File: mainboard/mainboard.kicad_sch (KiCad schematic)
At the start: 93 parts, among them J1 Eurorack_Power, J2 Inv1, J3 Inv2, J4 Ver2, J5 Ver1, J6 Conn_02x04_Counter_Clockwise, J7 Conn_02x03_Counter_Clockwise, J8 Out2, J9 Out1, Q1 BC557, Q10 BC557, Q11 BC557, Q12 BC557, Q13 BC547, Q14 BC547, Q15 BC557, Q16 BC557, Q17 BC547, Q18 BC547, Q19 BC557, Q2 BC557, Q20 BC557, Q21 BC547, Q22 BC547, Q23 BC557, Q24 BC547, Q25 BC547, Q3 BC547, Q4 BC547, Q5 BC547, Q6 BC547, Q7 BC547, Q8 BC547, Q9 BC557, U1 L78L09_TO92, U2 TL074

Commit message: Routing
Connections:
- net MIDO1: now also U2.6 (-), U2.7; no longer U2.1, U2.2 (-)
- net MIDO2: now also U2.8, U2.9 (-); no longer U2.13 (-), U2.14
- net Out1: now also U2.3 (+); no longer U2.5 (+)
- net at R13.2, R14.1: now also U2.5 (+); no longer U2.3 (+)
- net at C4.1, Q14.1 (C), R30.1: now also U2.12 (+); no longer U2.10 (+)
- net at R15.2, R16.1: now also U2.10 (+); no longer U2.12 (+)
- new net: R34.2, U2.1, U2.2 (-)
- new net: R33.2, U2.13 (-), U2.14
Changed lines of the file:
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@@
     (pin "1")
   )
-  (symbol (lib_id "Amplifier_Operational:TL074") (at 163.83 81.28 0) (unit 2)
+  (symbol (lib_id "Amplifier_Operational:TL074") (at 163.83 81.28 0) (unit 1)
     (in_bom yes) (on_board yes) (fields_autoplaced)
     (property "Reference" "U2" (id 0) (at 163.83 71.12 0))
@@
     (pin "3")
   )
-  (symbol (lib_id "Amplifier_Operational:TL074") (at 105.41 30.48 0) (unit 1)
+  (symbol (lib_id "Amplifier_Operational:TL074") (at 105.41 30.48 0) (unit 2)
     (in_bom yes) (on_board yes) (fields_autoplaced)
     (property "Reference" "U2" (id 0) (at 105.41 20.32 0))
@@
     (pin "6")
   )
-  (symbol (lib_id "Amplifier_Operational:TL074") (at 162.56 163.83 0) (unit 3)
+  (symbol (lib_id "Amplifier_Operational:TL074") (at 162.56 163.83 0) (unit 4)
     (in_bom yes) (on_board yes) (fields_autoplaced)
     (property "Reference" "U2" (id 0) (at 162.56 153.67 0))
@@
     (pin "3")
   )
-  (symbol (lib_id "Amplifier_Operational:TL074") (at 105.41 64.77 0) (unit 4)
+  (symbol (lib_id "Amplifier_Operational:TL074") (at 105.41 64.77 0) (unit 3)
     (in_bom yes) (on_board yes) (fields_autoplaced)
     (property "Reference" "U2" (id 0) (at 105.41 54.61 0))
@@
       (reference "U1") (unit 1) (value "L78L09_TO92") (footprint "Package_TO_SOT_THT:TO-92_Inline")
     )
+    (path "/0ebda1a3-7afe-4b2c-9147-5e2f0fea4082"
+      (reference "U2") (unit 1) (value "TL074") (footprint "Package_DIP:DIP-14_W7.62mm_Socket")
+    )
     (path "/211453b7-cfa5-409e-b9f2-b42bf15d1016"
-      (reference "U2") (unit 1) (value "TL074") (footprint "Package_DIP:DIP-14_W7.62mm_Socket")
-    )
-    (path "/0ebda1a3-7afe-4b2c-9147-5e2f0fea4082"
       (reference "U2") (unit 2) (value "TL074") (footprint "Package_DIP:DIP-14_W7.62mm_Socket")
     )
+    (path "/8cecb3d6-9653-4f3c-a3b3-a8676a225b3c"
+      (reference "U2") (unit 3) (value "TL074") (footprint "Package_DIP:DIP-14_W7.62mm_Socket")
+    )
     (path "/29c5794b-5b31-4263-a1f4-eb1defc43e42"
-      (reference "U2") (unit 3) (value "TL074") (footprint "Package_DIP:DIP-14_W7.62mm_Socket")
-    )
-    (path "/8cecb3d6-9653-4f3c-a3b3-a8676a225b3c"
       (reference "U2") (unit 4) (value "TL074") (footprint "Package_DIP:DIP-14_W7.62mm_Socket")
     )

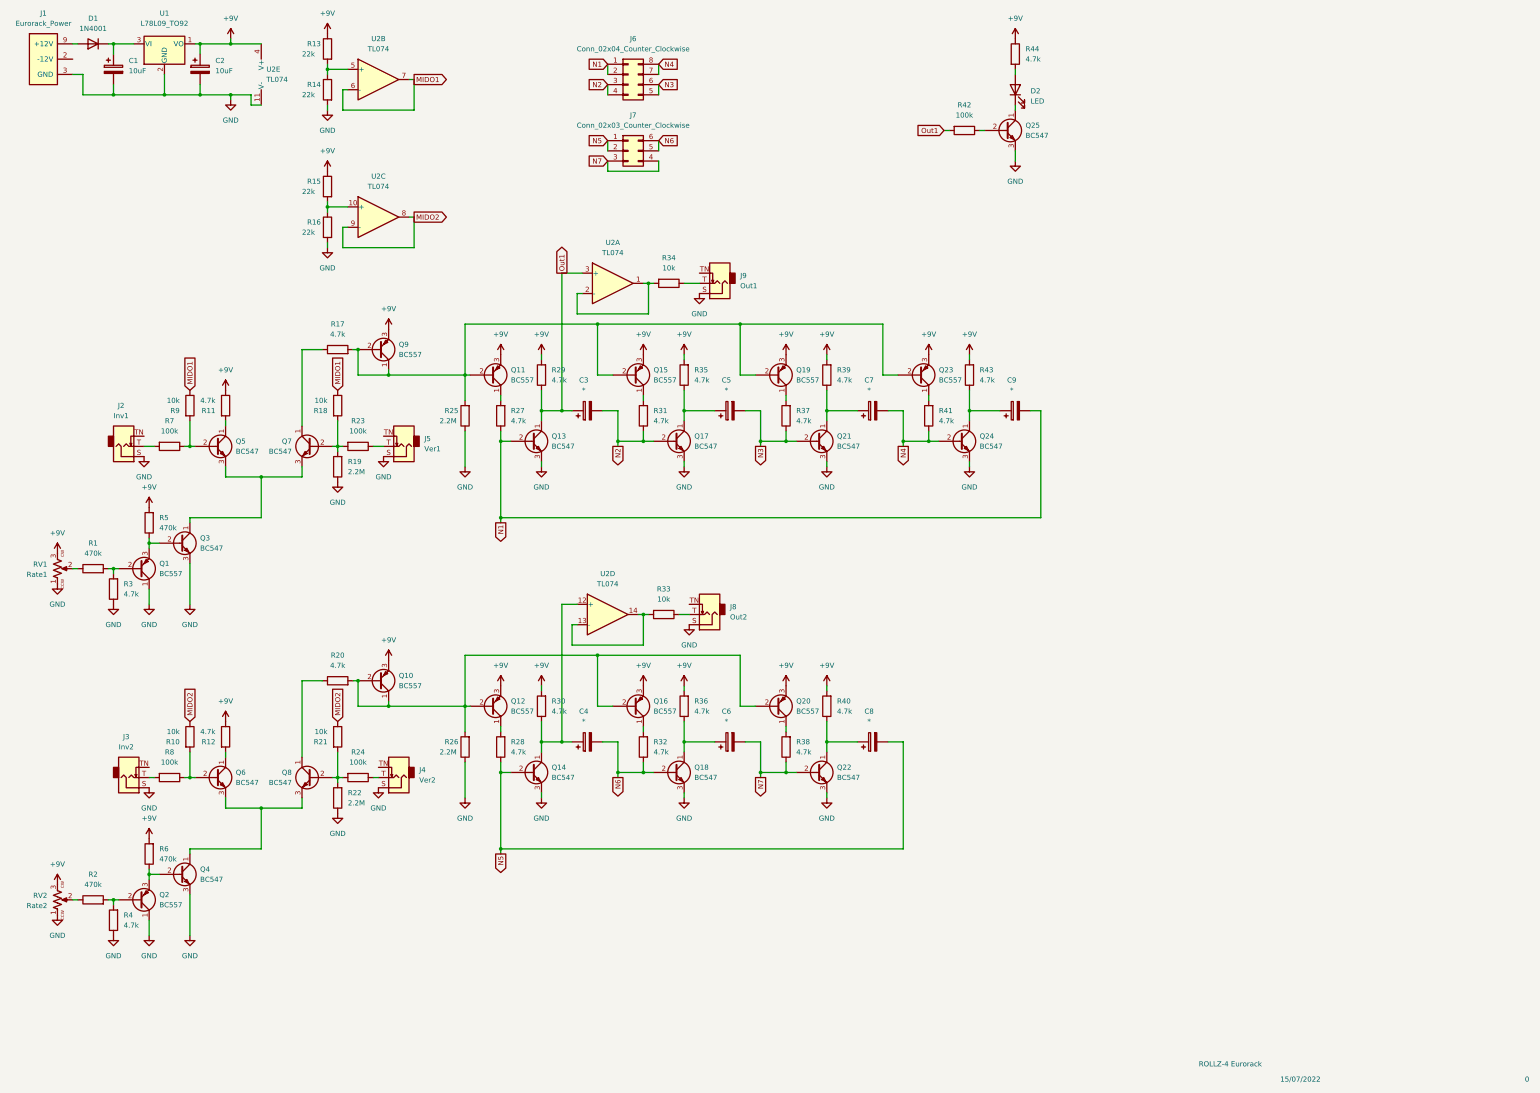
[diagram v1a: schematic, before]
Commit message: Attenuator version
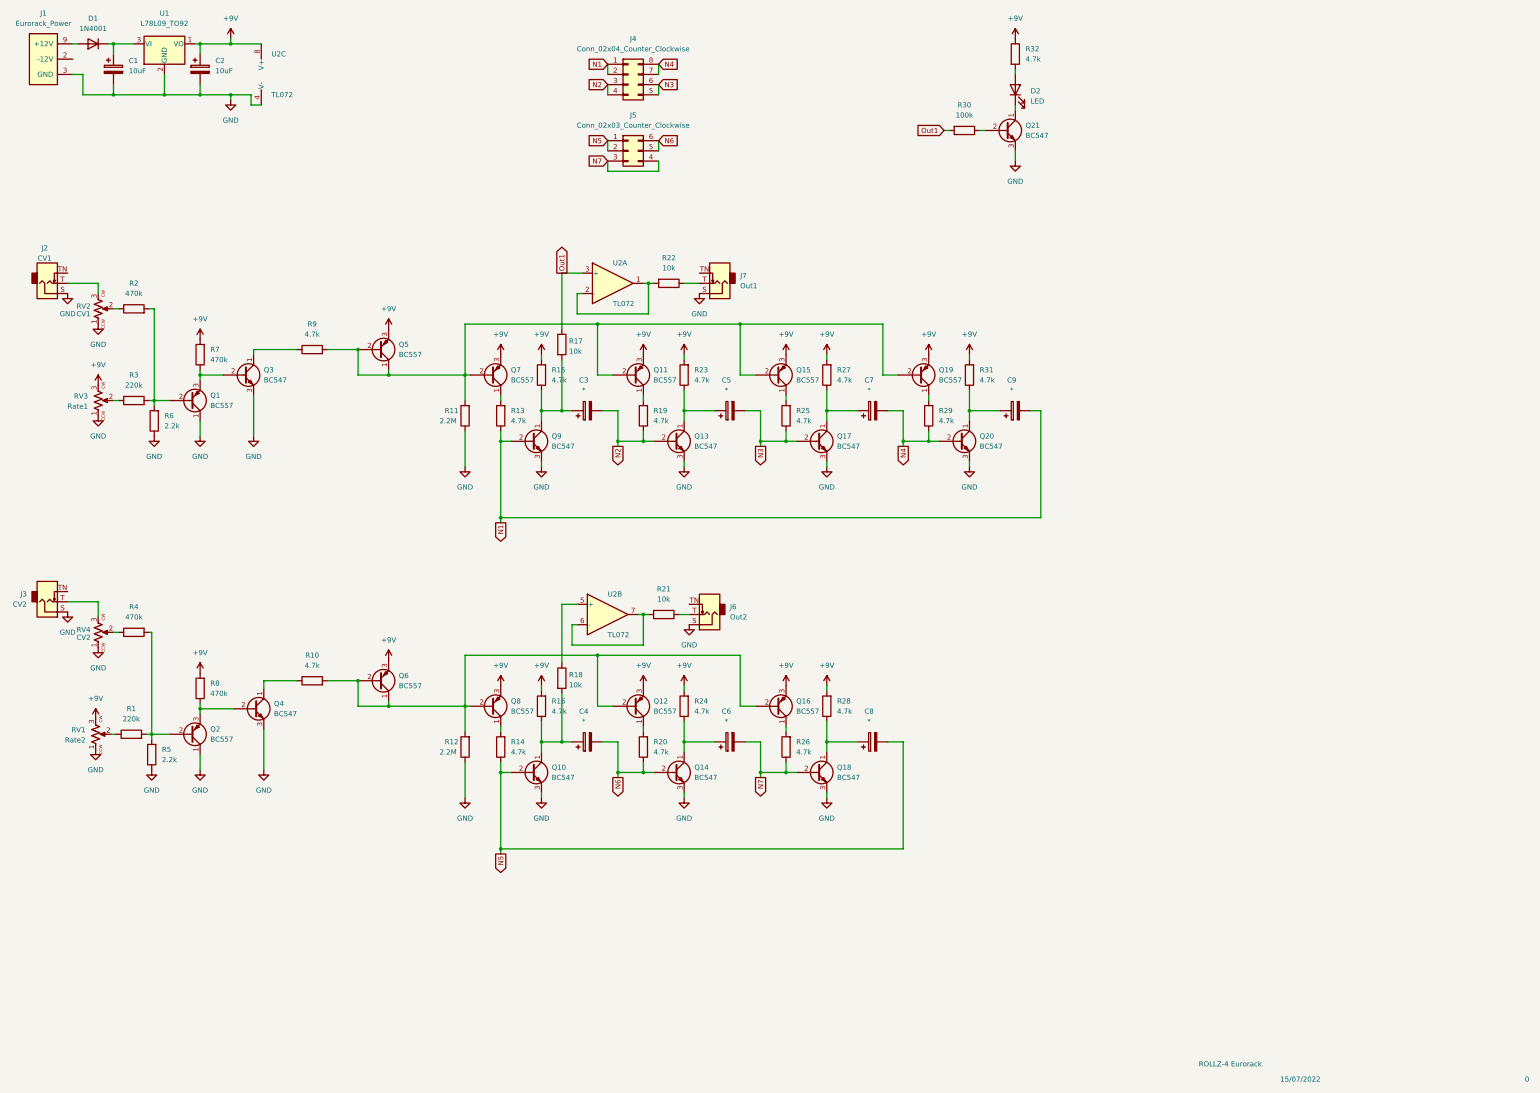
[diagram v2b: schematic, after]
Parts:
- removed J2: Inv1, winterbloom:AudioJack_WQP518MA, symbol winterbloom:Eurorack_Mono_Jack
- removed J3: Inv2, winterbloom:AudioJack_WQP518MA, symbol winterbloom:Eurorack_Mono_Jack
- removed Q5, Q6, Q7, Q8: BC547, Package_TO_SOT_THT:TO-92_Inline, symbol Transistor_BJT:BC547
- removed R10, R21, R9: 10k, Resistor_THT:R_Axial_DIN0204_L3.6mm_D1.6mm_P7.62mm_Horizontal, symbol Device:R
- removed R11, R12: 4.7k, Resistor_THT:R_Axial_DIN0204_L3.6mm_D1.6mm_P7.62mm_Horizontal, symbol Device:R
- removed R13, R14, R15, R16: 22k, Resistor_THT:R_Axial_DIN0204_L3.6mm_D1.6mm_P7.62mm_Horizontal, symbol Device:R
- removed R19, R22: 2.2M, Resistor_THT:R_Axial_DIN0204_L3.6mm_D1.6mm_P7.62mm_Horizontal, symbol Device:R
- removed R23, R7, R8: 100k, Resistor_THT:R_Axial_DIN0204_L3.6mm_D1.6mm_P7.62mm_Horizontal, symbol Device:R
- removed unit 2 of U2
- removed unit 3 of U2
- added R17: 10k, Resistor_THT:R_Axial_DIN0204_L3.6mm_D1.6mm_P7.62mm_Horizontal, symbol Device:R
- added R2: 470k, Resistor_THT:R_Axial_DIN0204_L3.6mm_D1.6mm_P7.62mm_Horizontal, symbol Device:R
- added RV2: CV1, winterbloom:Potentiometer_Alpha_R0904N, symbol winterbloom:Eurorack_Pot
- added RV4: CV2, winterbloom:Potentiometer_Alpha_R0904N, symbol winterbloom:Eurorack_Pot
- J2: renamed from J5; value Ver1 -> CV1
- J3: renamed from J4; value Ver2 -> CV2
- R1: renamed from R2; value 470k -> 220k
- R3: renamed from R1; value 470k -> 220k
- R4: renamed from R24; value 100k -> 470k
- R5: renamed from R4; value 4.7k -> 2.2k
- R6: renamed from R3; value 4.7k -> 2.2k
- U2: value TL074 -> TL072; footprint Package_DIP:DIP-14_W7.62mm_Socket -> Package_DIP:DIP-8_W7.62mm_Socket; symbol Amplifier_Operational:TL074 -> Amplifier_Operational:TL072
- renumbered J6 to J4, J7 to J5, J8 to J6, J9 to J7, Q14 to Q10, Q15 to Q11, Q16 to Q12, Q17 to Q13, Q18 to Q14, Q19 to Q15, Q20 to Q16, Q21 to Q17, Q22 to Q18, Q23 to Q19, Q24 to Q20, Q25 to Q21, Q9 to Q5, Q10 to Q6, Q11 to Q7, Q12 to Q8, Q13 to Q9, R20 to R10, R25 to R11, R26 to R12, R27 to R13, R28 to R14, R29 to R15, R30 to R16, R31 to R19, R32 to R20, R33 to R21, R34 to R22, R35 to R23, R36 to R24, R37 to R25, R38 to R26, R39 to R27, R40 to R28, R41 to R29, R42 to R30, R43 to R31, R44 to R32, R5 to R7, R6 to R8, R17 to R9, RV2 to RV1, RV1 to RV3
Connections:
- net +9V: now also U2.8 (V+); no longer U2.4 (V+)
- net GND: now also U2.4 (V-), RV2.1, RV4.1; no longer U2.11 (V-)
- net Out1: now also R17.1; no longer C3.1, Q9.1 (C), R15.1
- net at Q1.2 (B), R3.2, R6.2: now also R2.2
- net at R4.1: now also RV4.2; no longer J3.T (Tip)
- net at R4.2: now also Q2.2 (B), R1.2, R5.2
- net at R10.1: now also Q4.1 (C)
- net at C4.1, Q10.1 (C), R16.1: now also R18.2; no longer U2.12 (+)
- net at Q3.1 (C): now also R9.1
- net at J2.T (Tip): now also RV2.3
- net MIDO1: no longer names the net of R18.1
- net MIDO1: now also U2.5 (+)
- new net: R2.1, RV2.2
- new net: C3.1, Q9.1 (C), R15.1, R17.2
- new net: R21.2, U2.6 (-), U2.7
- new net: J3.T (Tip), RV4.3
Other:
- moved on the sheet: J2, J3, Q1, Q2, Q3, Q4, R1, R10, R3, R4, R5, R6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

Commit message: Front panel
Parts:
- added D3, D4: BAT85, Diode_THT:D_DO-35_SOD27_P7.62mm_Horizontal, symbol Diode:BAT85
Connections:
- net GND: now also D3.2 (A), D4.2 (A)
- net at J2.T (Tip), RV2.3: now also D3.1 (K)
- net at J3.T (Tip), RV4.3: now also D4.1 (K)
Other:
- moved on the sheet: C3, C4, C5, C6, C7, C8, C9, J2, J3, J6, J7, Q1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

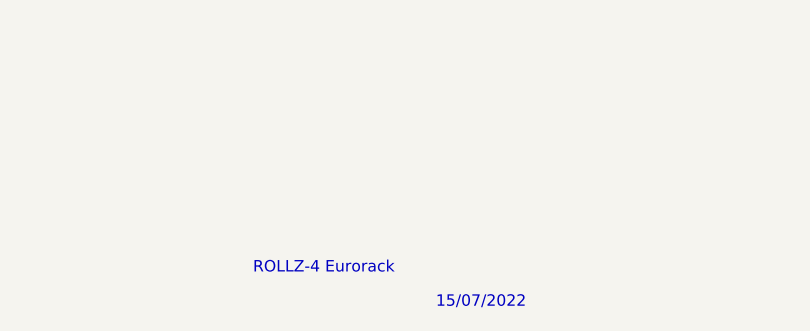
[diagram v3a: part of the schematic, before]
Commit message: Changes to references
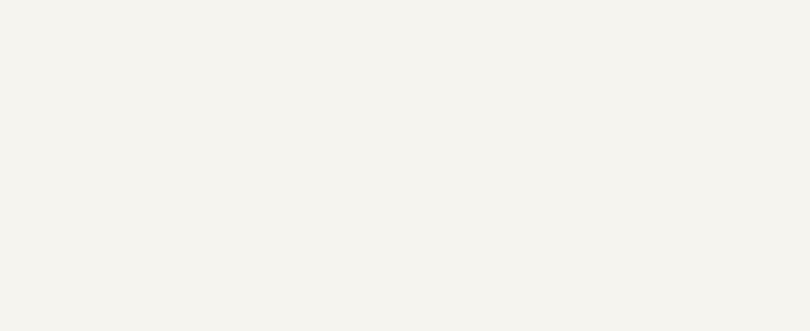
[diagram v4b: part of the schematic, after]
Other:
- note removed: "15/07/2022"
- note removed: "ROLLZ-4 Eurorack"
- title: (none) -> Rollz 4 Euro
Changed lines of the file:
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@@
 (kicad_sch (version 20211123) (generator eeschema)
   (paper "A3")
+  (title_block
+    (title "Rollz 4 Euro")
+  )
   (junction (at 149.225 142.24) (diameter 0) (color 0 0 0 0)
   )
@@
   (wire (pts (xy 184.785 123.19) (xy 184.785 120.65))
     (stroke (width 0) (type default) (color 0 0 0 0))
-  )
-  (text "ROLLZ-4 Eurorack" (at 309.88 276.86 0)
-    (effects (font (size 1.27 1.27)) (justify left bottom))
   )
   (text "0" (at 391.16 280.67 0)
     (effects (font (size 1.27 1.27)) (justify left bottom))
   )
-  (text "15/07/2022" (at 330.2 280.67 0)
-    (effects (font (size 1.27 1.27)) (justify left bottom))
-  )
